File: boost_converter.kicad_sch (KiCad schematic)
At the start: 13 parts, among them U1 TPS61170DRVR

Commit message: laid out stuff
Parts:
- added D2: RED LED, LED_SMD:LED_0805_2012Metric_Pad1.15x1.40mm_HandSolder, symbol Device:LED_Filled
- added R29: 300K, Resistor_SMD:R_0805_2012Metric_Pad1.20x1.40mm_HandSolder, symbol Device:R
- added TP1: 5264 (Yellow), TestPoint:TestPoint_Keystone_5000-5004_Miniature, symbol Connector:TestPoint
- added TP3: 5261 (Black), TestPoint:TestPoint_Keystone_5000-5004_Miniature, symbol Connector:TestPoint
- C2: footprint rgb_led_driver_footprints:EEHZA1J100P -> Capacitor_SMD:CP_Elec_6.3x5.8; MPN (none) -> EEH-ZA1J100P
- U1: Availability In Stock -> (none); Check_prices https://www.snapeda.com/parts/TPS61170DRVR/Texas+Instrument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 -> (none); MF Texas Instruments -> (none); MP TPS61170DRVR -> (none); Package WSON-6 Texas Instruments -> (none); Price None -> (none); Purchase-URL https://www.snapeda.com/api/url_track_click_mouser/?unipart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 -> (none); SnapEDA_Link https://www.snapeda.com/parts/TPS61170DRVR/Texas+Instrument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 -> (none)
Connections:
- net GND: now also R29.1, TP3.1
- net VOUT: now also D2.2 (A), TP1.1
- new net: D2.1 (K), R29.2

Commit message: neat-ified schematics
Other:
- company: (none) -> The Art and Science of PCB Design
- title: (none) -> RGB LED Driver Demo Board
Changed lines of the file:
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@@
   (paper "USLetter")
   (title_block
+    (title "RGB LED Driver Demo Board")
     (date "2024-01-01")
     (rev "A01")
+    (company "The Art and Science of PCB Design")
   )
   (junction (at 163.83 86.36) (diameter 0) (color 0 0 0 0)

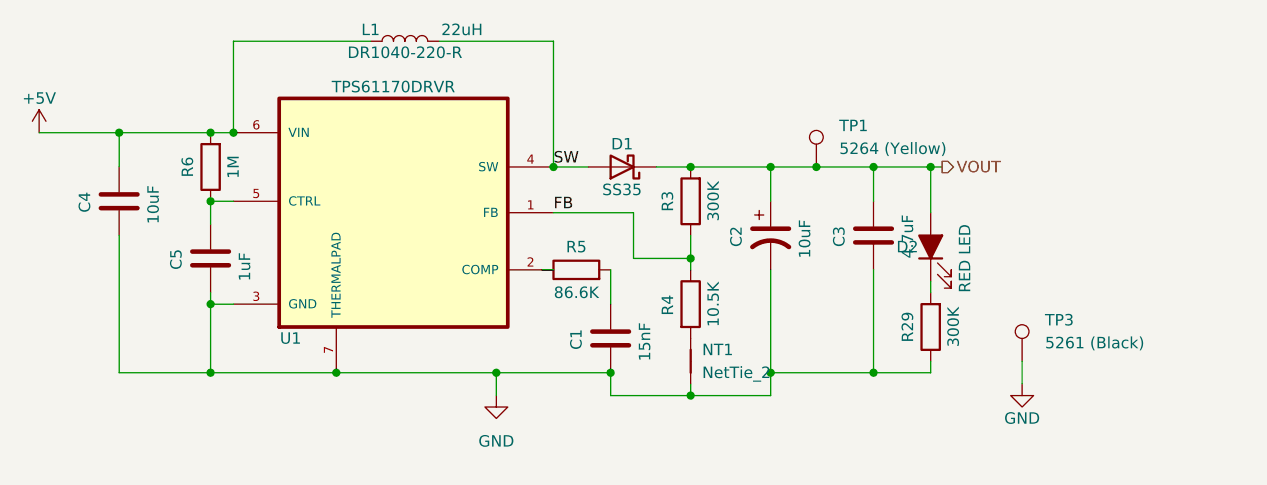
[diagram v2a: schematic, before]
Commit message: Added annotations, BOM count reduction
LED indicator resistors edited to save on BOM count

schematics made more neat, added some labels
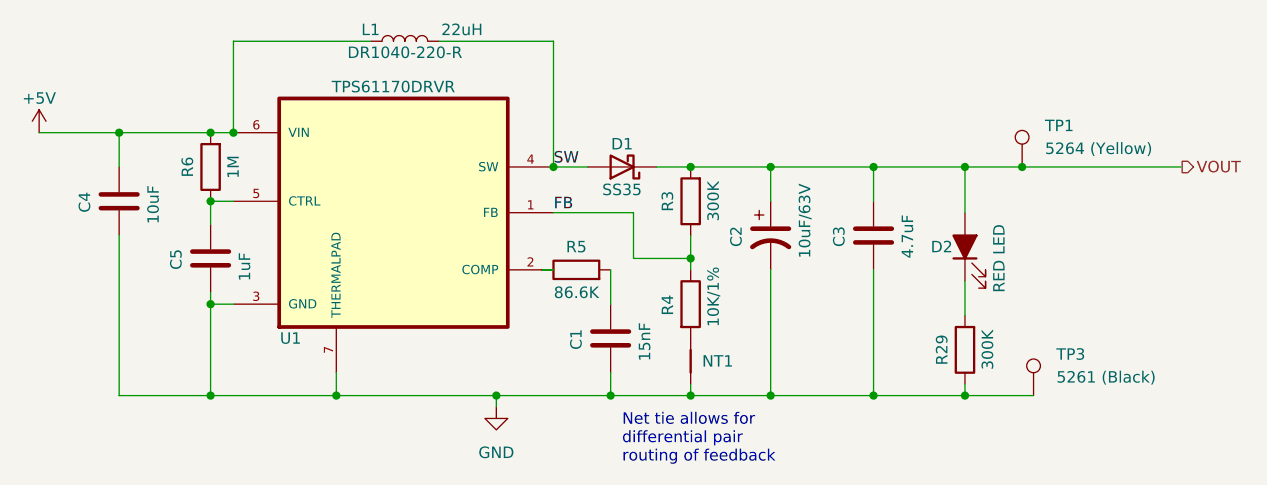
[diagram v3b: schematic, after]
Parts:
- C2: value 10uF -> 10uF/63V
- NT1: value NetTie_2 -> Nettie
- R4: value 10.5K -> 10K/1%
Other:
- note added: "Net tie allows for differential pair routing of feedback"
- moved on the sheet: D2, R29, TP1, TP3

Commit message: added digikey PNs
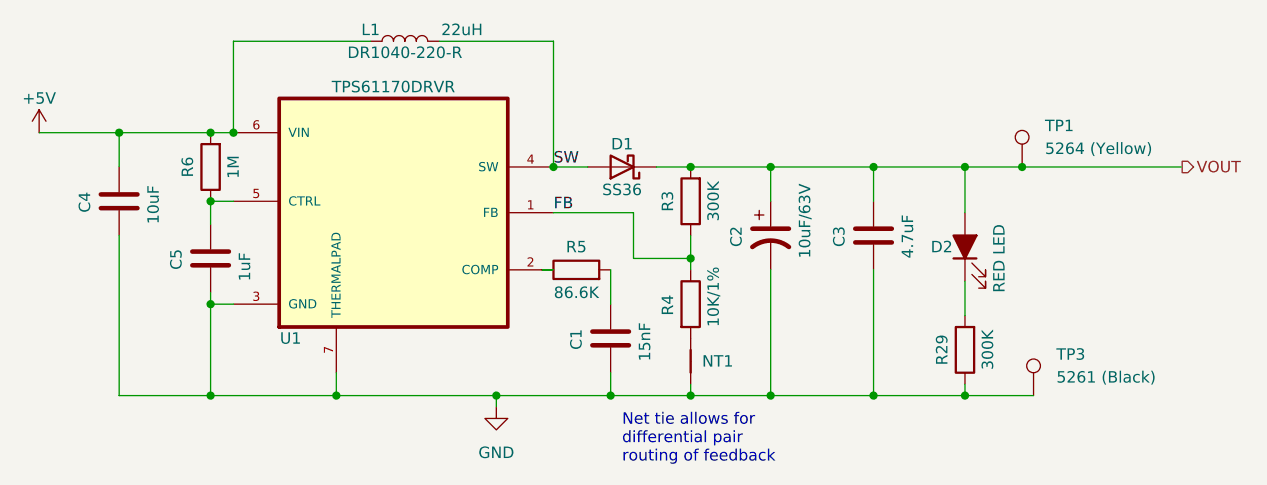
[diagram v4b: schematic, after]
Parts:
- C1: Digikey PN (none) -> 399-C0805C153G5GEC7800TR-ND; MPN (none) -> C0805C153G5GEC7800
- C2: Digikey PN (none) -> P15446TR-ND
- C3: Digikey PN (none) -> 445-5980-1-ND; MPN (none) -> C2012X5R1H475K125AB
- C4: Digikey PN (none) -> 1276-6454-1-ND; MPN (none) -> CL21A106KAYNNNG
- C5: Digikey PN (none) -> 1276-1003-1-ND; MPN (none) -> CL21B104KBCNNNC
- D1: value SS35 -> SS36; Digikey PN (none) -> 1801-SS36CT-ND; MPN SS35 -> SS36
- D2: Digikey PN (none) -> 160-1427-1-ND; MPN (none) -> LTST-C171KRKT
- L1: Digikey PN (none) -> DR1040-220-R
- R6: MPN (none) -> 0805W8F1004
- TP1: Digikey PN (none) -> 36-5264-ND; MPN (none) -> 5264
- TP3: Digikey PN (none) -> 36-5261-ND; MPN (none) -> 5261
- U1: Digikey PN (none) -> 296-22945-1-ND; MPN (none) -> TPS61170DRVR
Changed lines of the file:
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@@
       (effects (font (size 1.27 1.27)))
     )
-    (property "Value" "SS35" (at 171.45 88.9 0)
+    (property "Value" "SS36" (at 171.45 88.9 0)
       (effects (font (size 1.27 1.27)))
     )
@@
       (effects (font (size 1.27 1.27)) hide)
     )
-    (property "Datasheet" "https://www.onsemi.com/pdf/datasheet/ss39-d.pdf" (at 171.45 86.36 0)
-      (effects (font (size 1.27 1.27)) hide)
-    )
-    (property "MPN" "SS35" (at 171.45 86.36 0)
-      (effects (font (size 1.27 1.27)) hide)
-    )
-    (property "Digikey PN" "" (at 171.45 86.36 0)
+    (property "Datasheet" "https://services.ts.com.tw/storage/resources/datasheet/SS32%20SERIES_O2102.pdf" (at 171.45 86.36 0)
+      (effects (font (size 1.27 1.27)) hide)
+    )
+    (property "MPN" "SS36" (at 171.45 86.36 0)
+      (effects (font (size 1.27 1.27)) hide)
+    )
+    (property "Digikey PN" "1801-SS36CT-ND" (at 171.45 86.36 0)
       (effects (font (size 1.27 1.27)) hide)
     )
@@
       (effects (font (size 1.27 1.27)) hide)
     )
-    (property "Digikey PN" "" (at 199.39 93.98 0)
+    (property "Digikey PN" "445-5980-1-ND" (at 199.39 93.98 0)
+      (effects (font (size 1.27 1.27)) hide)
+    )
+    (property "MPN" "C2012X5R1H475K125AB" (at 199.39 93.98 0)
       (effects (font (size 1.27 1.27)) hide)
     )
@@
       (effects (font (size 1.27 1.27)) hide)
     )
-    (property "Digikey PN" "" (at 209.55 95.25 0)
+    (property "Digikey PN" "160-1427-1-ND" (at 209.55 95.25 0)
+      (effects (font (size 1.27 1.27)) hide)
+    )
+    (property "MPN" "LTST-C171KRKT" (at 209.55 95.25 0)
       (effects (font (size 1.27 1.27)) hide)
     )
@@
       (effects (font (size 1.27 1.27)) hide)
     )
+    (property "MPN" "0805W8F1004" (at 125.73 86.36 0)
+      (effects (font (size 1.27 1.27)) hide)
+    )
     (pin "1")
     (pin "2")
@@
       (effects (font (size 1.27 1.27)) hide)
     )
-    (property "Digikey PN" "" (at 170.18 105.41 0)
+    (property "Digikey PN" "399-C0805C153G5GEC7800TR-ND" (at 170.18 105.41 0)
+      (effects (font (size 1.27 1.27)) hide)
+    )
+    (property "MPN" "C0805C153G5GEC7800" (at 170.18 105.41 0)
       (effects (font (size 1.27 1.27)) hide)
     )
@@
       (effects (font (size 1.27 1.27)) hide)
     )
-    (property "Digikey PN" "" (at 215.9 86.36 0)
+    (property "Digikey PN" "36-5264-ND" (at 215.9 86.36 0)
+      (effects (font (size 1.27 1.27)) hide)
+    )
+    (property "MPN" "5264" (at 215.9 86.36 0)
       (effects (font (size 1.27 1.27)) hide)
     )
@@
       (effects (font (size 1.27 1.27)))
     )
-    (property "Digikey PN" "" (at 147.32 72.39 0)
+    (property "Digikey PN" "DR1040-220-R" (at 147.32 72.39 0)
       (effects (font (size 1.27 1.27)) hide)
     )
@@
       (effects (font (size 1.27 1.27)) hide)
     )
-    (property "Digikey PN" "" (at 125.73 96.52 0)
+    (property "Digikey PN" "1276-1003-1-ND" (at 125.73 96.52 0)
+      (effects (font (size 1.27 1.27)) hide)
+    )
+    (property "MPN" "CL21B104KBCNNNC" (at 125.73 96.52 0)
       (effects (font (size 1.27 1.27)) hide)
     )
@@
       (effects (font (size 1.27 1.27)) hide)
     )
-    (property "Digikey PN" "" (at 217.17 111.76 0)
+    (property "Digikey PN" "36-5261-ND" (at 217.17 111.76 0)
+      (effects (font (size 1.27 1.27)) hide)
+    )
+    (property "MPN" "5261" (at 217.17 111.76 0)
       (effects (font (size 1.27 1.27)) hide)
     )
@@
       (effects (font (size 1.27 1.27)) hide)
     )
-    (property "Digikey PN" "" (at 115.57 90.17 0)
+    (property "Digikey PN" "1276-6454-1-ND" (at 115.57 90.17 0)
+      (effects (font (size 1.27 1.27)) hide)
+    )
+    (property "MPN" "CL21A106KAYNNNG" (at 115.57 90.17 0)
       (effects (font (size 1.27 1.27)) hide)
     )
@@
       (effects (font (size 1.27 1.27)) hide)
     )
-    (property "Digikey PN" "" (at 146.05 91.44 0)
+    (property "Digikey PN" "296-22945-1-ND" (at 146.05 91.44 0)
+      (effects (font (size 1.27 1.27)) hide)
+    )
+    (property "MPN" "TPS61170DRVR" (at 146.05 91.44 0)
       (effects (font (size 1.27 1.27)) hide)
     )
@@
       (effects (font (size 1.27 1.27)) hide)
     )
-    (property "Digikey PN" "" (at 187.96 93.98 0)
-      (effects (font (size 1.27 1.27)) hide)
-    )
+    (property "Digikey PN" "P15446TR-ND" (at 187.96 93.98 0)
+      (effects (font (size 1.27 1.27)) hide)
+    )

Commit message: added digikey PNs to all devices
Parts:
- C1: Digikey PN 399-C0805C153G5GEC7800TR-ND -> 399-C0805C153G5GEC7800CT-ND
- C2: Digikey PN P15446TR-ND -> P15446CT-ND
- L1: Digikey PN DR1040-220-R -> 513-1401-1-ND
- R29, R3: Digikey PN (none) -> RMCF0805FT300KCT-ND; MPN (none) -> RMCF0805FT300K
- R4: Digikey PN (none) -> RMCF0805FT10K0CT-ND; MPN (none) -> RMCF0805FT10K0
- R5: Digikey PN (none) -> RMCF0805FT86K6CT-ND; MPN (none) -> RMCF0805FT86K6
- R6: Digikey PN (none) -> RMCF0805FT1M00CT-ND; MPN 0805W8F1004 -> RMCF0805FT1M00
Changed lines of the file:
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@@
       (effects (font (size 1.27 1.27)) hide)
     )
-    (property "Digikey PN" "" (at 179.07 90.17 0)
+    (property "Digikey PN" "RMCF0805FT300KCT-ND" (at 179.07 90.17 0)
+      (effects (font (size 1.27 1.27)) hide)
+    )
+    (property "MPN" "RMCF0805FT300K" (at 179.07 90.17 0)
       (effects (font (size 1.27 1.27)) hide)
     )
@@
       (effects (font (size 1.27 1.27)) hide)
     )
-    (property "Digikey PN" "" (at 209.55 106.68 0)
+    (property "Digikey PN" "RMCF0805FT300KCT-ND" (at 209.55 106.68 0)
+      (effects (font (size 1.27 1.27)) hide)
+    )
+    (property "MPN" "RMCF0805FT300K" (at 209.55 106.68 0)
       (effects (font (size 1.27 1.27)) hide)
     )
@@
       (effects (font (size 1.27 1.27)) hide)
     )
-    (property "Digikey PN" "" (at 125.73 86.36 0)
-      (effects (font (size 1.27 1.27)) hide)
-    )
-    (property "MPN" "0805W8F1004" (at 125.73 86.36 0)
+    (property "Digikey PN" "RMCF0805FT1M00CT-ND" (at 125.73 86.36 0)
+      (effects (font (size 1.27 1.27)) hide)
+    )
+    (property "MPN" "RMCF0805FT1M00" (at 125.73 86.36 0)
       (effects (font (size 1.27 1.27)) hide)
     )
@@
       (effects (font (size 1.27 1.27)) hide)
     )
-    (property "Digikey PN" "399-C0805C153G5GEC7800TR-ND" (at 170.18 105.41 0)
+    (property "Digikey PN" "399-C0805C153G5GEC7800CT-ND" (at 170.18 105.41 0)
       (effects (font (size 1.27 1.27)) hide)
     )
@@
       (effects (font (size 1.27 1.27)))
     )
-    (property "Digikey PN" "DR1040-220-R" (at 147.32 72.39 0)
+    (property "Digikey PN" "513-1401-1-ND" (at 147.32 72.39 0)
       (effects (font (size 1.27 1.27)) hide)
     )
@@
       (effects (font (size 1.27 1.27)) hide)
     )
-    (property "Digikey PN" "" (at 166.37 97.79 0)
+    (property "Digikey PN" "RMCF0805FT86K6CT-ND" (at 166.37 97.79 0)
+      (effects (font (size 1.27 1.27)) hide)
+    )
+    (property "MPN" "RMCF0805FT86K6" (at 166.37 97.79 0)
       (effects (font (size 1.27 1.27)) hide)
     )
@@
       (effects (font (size 1.27 1.27)) hide)
     )
-    (property "Digikey PN" "" (at 179.07 101.6 0)
+    (property "Digikey PN" "RMCF0805FT10K0CT-ND" (at 179.07 101.6 0)
+      (effects (font (size 1.27 1.27)) hide)
+    )
+    (property "MPN" "RMCF0805FT10K0" (at 179.07 101.6 0)
       (effects (font (size 1.27 1.27)) hide)
     )
@@
       (effects (font (size 1.27 1.27)) hide)
     )
-    (property "Digikey PN" "P15446TR-ND" (at 187.96 93.98 0)
-      (effects (font (size 1.27 1.27)) hide)
-    )
+    (property "Digikey PN" "P15446CT-ND" (at 187.96 93.98 0)
+      (effects (font (size 1.27 1.27)) hide)
+    )

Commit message: cost reduction in BOM
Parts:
- C1: Digikey PN 399-C0805C153G5GEC7800CT-ND -> 399-C0805C153K5RAC7800CT-ND; MPN C0805C153G5GEC7800 -> C0805C153K5RAC7800
- C5: Digikey PN 1276-1003-1-ND -> 1276-1029-1-ND; MPN CL21B104KBCNNNC -> CL21B105KBFNNNE
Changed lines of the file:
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@@
       (effects (font (size 1.27 1.27)) hide)
     )
-    (property "Digikey PN" "399-C0805C153G5GEC7800CT-ND" (at 170.18 105.41 0)
+    (property "Digikey PN" "399-C0805C153K5RAC7800CT-ND" (at 170.18 105.41 0)
       (effects (font (size 1.27 1.27)) hide)
     )
-    (property "MPN" "C0805C153G5GEC7800" (at 170.18 105.41 0)
+    (property "MPN" "C0805C153K5RAC7800" (at 170.18 105.41 0)
       (effects (font (size 1.27 1.27)) hide)
     )
@@
       (effects (font (size 1.27 1.27)) hide)
     )
-    (property "Digikey PN" "1276-1003-1-ND" (at 125.73 96.52 0)
+    (property "Digikey PN" "1276-1029-1-ND" (at 125.73 96.52 0)
       (effects (font (size 1.27 1.27)) hide)
     )
-    (property "MPN" "CL21B104KBCNNNC" (at 125.73 96.52 0)
+    (property "MPN" "CL21B105KBFNNNE" (at 125.73 96.52 0)
       (effects (font (size 1.27 1.27)) hide)
     )

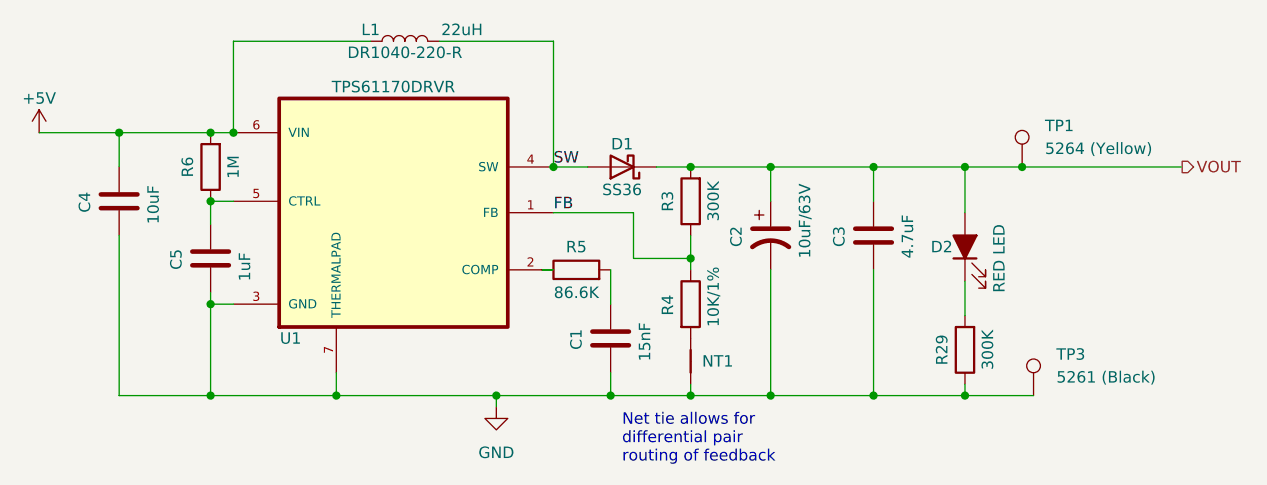
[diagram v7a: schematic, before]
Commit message: [A02] Edited resistor values
R11 to 51K to allow for auto reset
R3 to 270K for 34V output
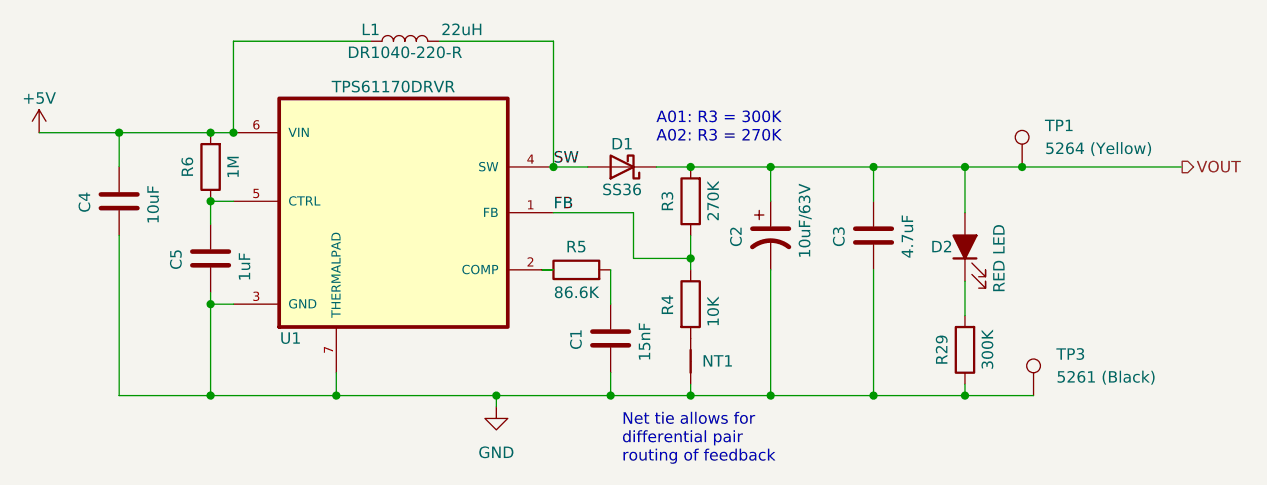
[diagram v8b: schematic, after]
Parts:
- R3: value 300K -> 270K
- R4: value 10K/1% -> 10K
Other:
- note added: "A01: R3 = 300K A02: R3 = 270K"
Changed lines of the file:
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@@
+    (effects (font (size 1.27 1.27)) (justify left bottom))
+  )
+  (text "A01: R3 = 300K\nA02: R3 = 270K" (at 175.26 83.82 0)
     (effects (font (size 1.27 1.27)) (justify left bottom))
   )
@@
       (effects (font (size 1.27 1.27)))
     )
-    (property "Value" "300K" (at 181.61 90.17 90)
+    (property "Value" "270K" (at 181.61 90.17 90)
       (effects (font (size 1.27 1.27)))
     )
@@
       (effects (font (size 1.27 1.27)) (justify left))
     )
-    (property "Value" "10K/1%" (at 181.61 104.14 90)
-      (effects (font (size 1.27 1.27)) (justify left))
-    )
+    (property "Value" "10K" (at 181.61 104.14 90)
+      (effects (font (size 1.27 1.27)) (justify left))
+    )
